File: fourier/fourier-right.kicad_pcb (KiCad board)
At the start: 2 copper layers, 129.2 x 73.8 mm, 123 parts, among them J1 VCC, J3 RGB, J6 C6, J7 GND, T1 TRRS, U1 ProMicro

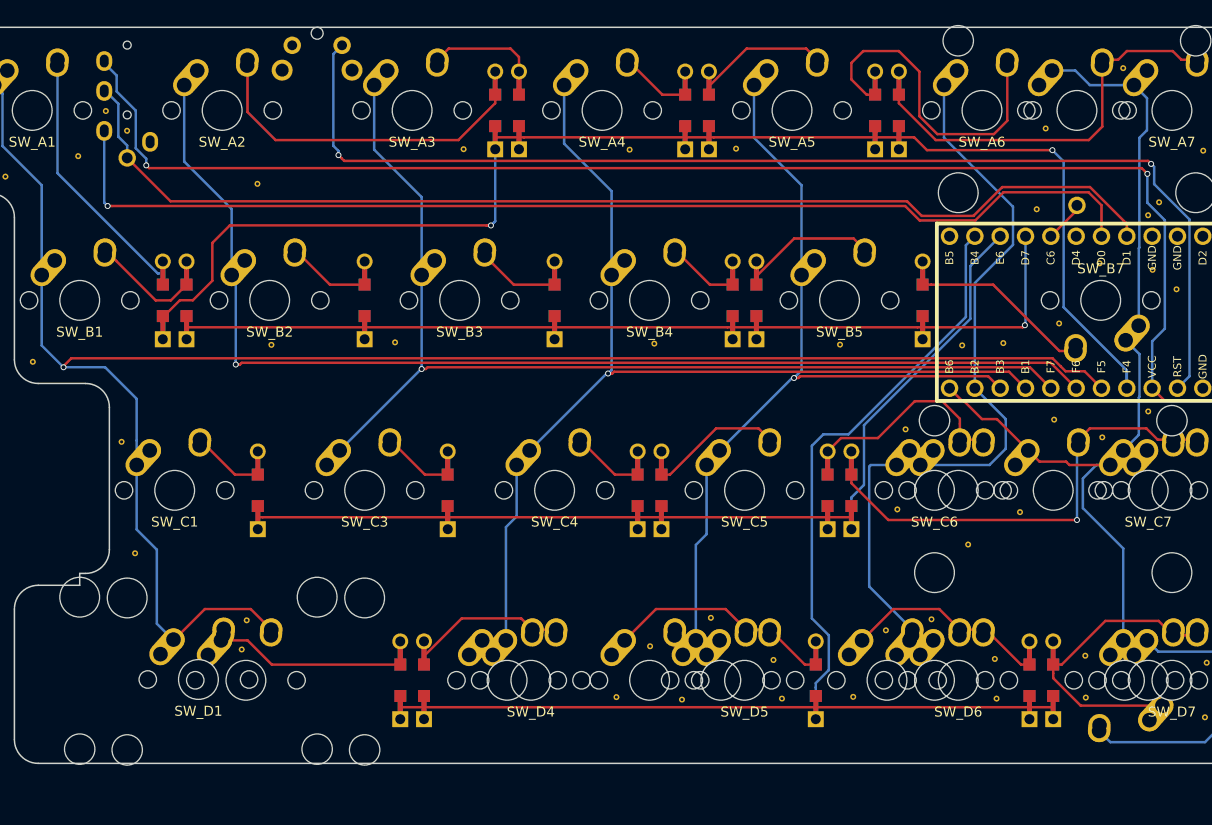
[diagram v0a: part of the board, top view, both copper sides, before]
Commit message: Add mounting holes to right side
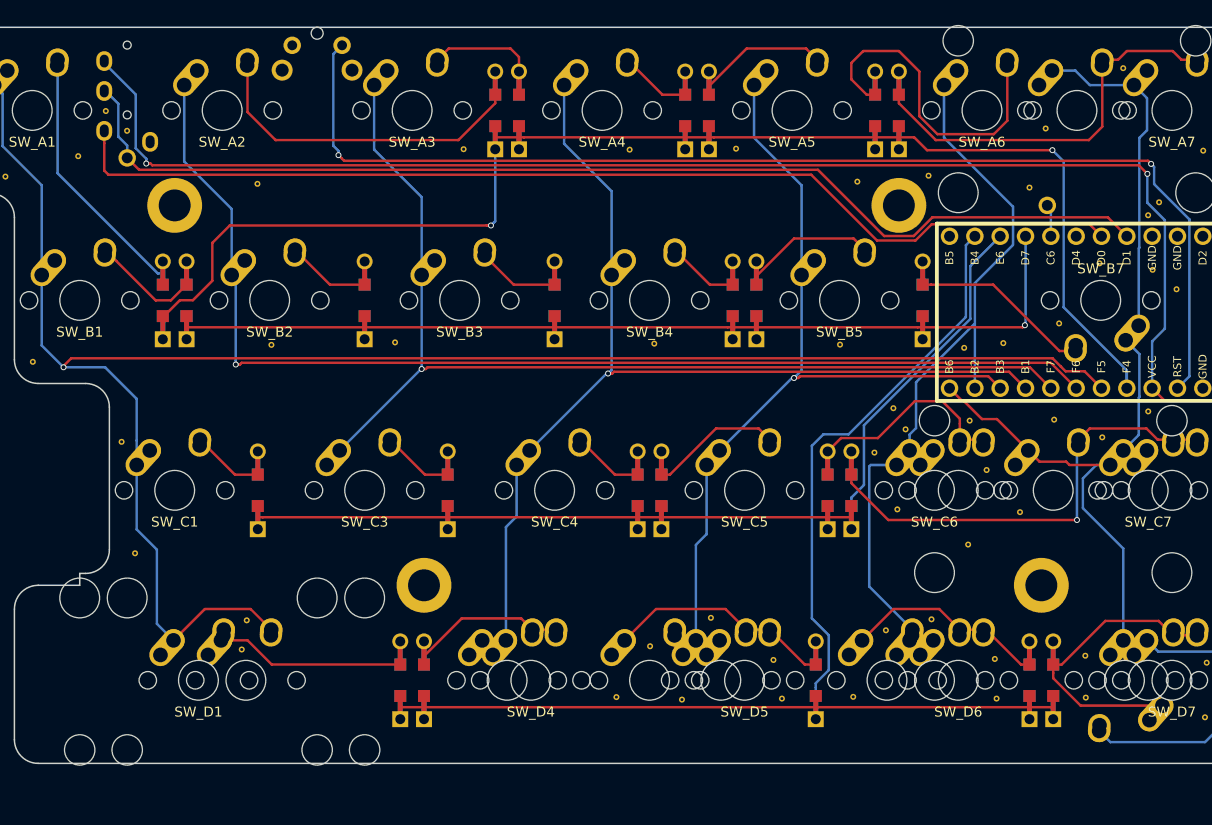
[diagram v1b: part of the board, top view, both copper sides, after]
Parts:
- added REF**: VIA-0.6mm, Keebio-Parts:VIA-0.6mm, F.Cu at (127.4, 64.5)
- added REF**: VIA-0.6mm, Keebio-Parts:VIA-0.6mm, F.Cu at (129.1, 69.4)
- added REF**: VIA-0.6mm, Keebio-Parts:VIA-0.6mm, F.Cu at (117.8, 67.7)
- added REF**: VIA-0.6mm, Keebio-Parts:VIA-0.6mm, F.Cu at (119.7, 63.2)
- added REF**: VIA-0.6mm, Keebio-Parts:VIA-0.6mm, F.Cu at (123.2, 39.9)
- added REF**: VIA-0.6mm, Keebio-Parts:VIA-0.6mm, F.Cu at (116.1, 40.5)
- added REF**: MountingHole_3.2mm_M3_ISO14580_Pad, Mounting_Holes:MountingHole_3.2mm_M3_ISO14580_Pad, F.Cu at (134.5, 81.0)
- added REF**: MountingHole_3.2mm_M3_ISO14580_Pad, Mounting_Holes:MountingHole_3.2mm_M3_ISO14580_Pad, F.Cu at (120.3, 42.9)
- added REF**: MountingHole_3.2mm_M3_ISO14580_Pad, Mounting_Holes:MountingHole_3.2mm_M3_ISO14580_Pad, F.Cu at (47.6, 42.9)
- added REF**: MountingHole_3.2mm_M3_ISO14580_Pad, Mounting_Holes:MountingHole_3.2mm_M3_ISO14580_Pad, F.Cu at (72.6, 81.0)
- moved J6 2.98 mm to (135.1, 42.9)
- moved REF** 2.29 mm to (133.4, 41.1)
- moved REF** 0.32 mm to (126.8, 57.1)
- moved SW_D1 0.08 mm to (50.0, 90.5)
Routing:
- net data: track 112.8 -> 108.1 mm, vias 1 -> 0
- net data2: track 114.4 -> 112.8 mm
- net col6: track 77.2 -> 76.0 mm
- net C6: track 4.18 -> 3.24 mm
